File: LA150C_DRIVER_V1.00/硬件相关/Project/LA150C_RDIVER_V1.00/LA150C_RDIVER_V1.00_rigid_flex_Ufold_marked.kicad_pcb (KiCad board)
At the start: 2 copper layers, 21 x 11 mm, 5 parts, among them U1 SCT2230MLUAR, U2 GD32F503REL7, U3 MP6543HGL-Z, U4 MT6701, U5 TCAN3413DDFR

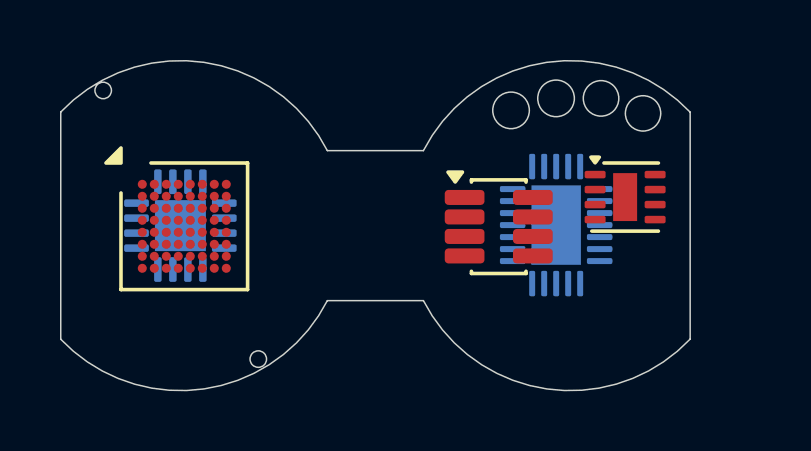
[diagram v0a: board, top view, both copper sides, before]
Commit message: Add LA150C rigid-flex U-fold board, ECLGA footprint and KZ11 assembly
- FPC widened to 5.202 mm, 4 mm bend band, R0.5 U-fold, bottom copper outside
- SCT2230MLUAR rebuilt as ECLGA2.5X1.7-7L with matching 3D body
- folded board placed into the KZ11 structure assembly
- generator scripts for FPC, footprint, 3D and assembly
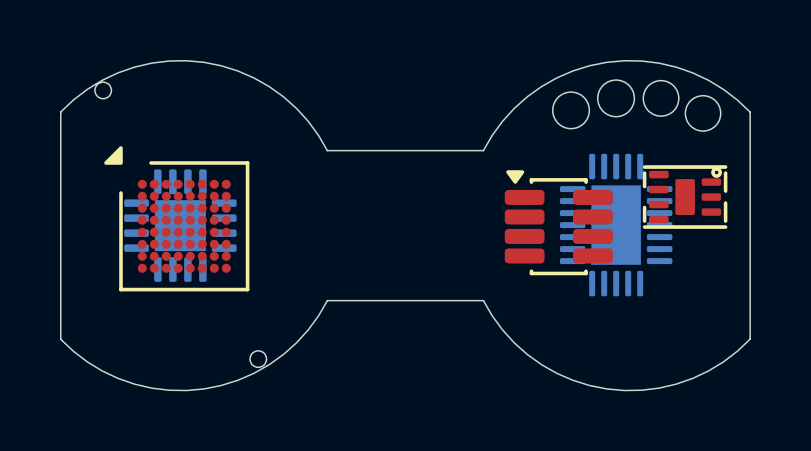
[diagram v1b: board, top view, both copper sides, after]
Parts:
- U1: footprint DFN-8-1EP_2x2mm_P0.5mm_EP0.8x1.6mm -> LA150C_RDIVER_V1.00:ECLGA2.5X1.7-7L
- moved U1 2.00 mm to (116.8, 99.0)
- moved U3 2.00 mm to (114.5, 100.0)
- moved U5 2.00 mm to (112.6, 100.0)
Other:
- board size 21 x 11 mm -> 23 x 11 mm
- board text added: "FPC 0.2 mm (5.202 x 5.0)"
- board text added: "FPC bottom Cu: outside (convex) top Cu: inside (concave)"
- board text added: "U-FOLD 180deg R=0.5mm bend lines FPC centre +/-2.0mm"
- board text removed: "FPC 0.2 mm"
- board text removed: "U-FOLD AXIS 180 deg, R=1.019 mm"
